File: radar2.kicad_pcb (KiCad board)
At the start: 4 copper layers, 103.4 x 65 mm, 135 parts, among them IC1 BQ25713RSNR, IC2 TPS54540DDA, IC3 LP5907QMFX-3.0Q1, IC5 LP5907QMFX-3.0Q1, IC6 DW3220TR13, J1 GSB1C4621DS1HR, J2 M20-8770546 (for SWD), J3 M20-9730446_DISPLAY_POWER, J4 JST-XH, J5 M20-9990646_PI, J6 SMA_CONNECTOR, J7 SMA_CONNECTOR, Q1 CSD17308Q3, Q2 CSD17308Q3, Q3 CSD17308Q3, Q4 CSD17308Q3, Q5 CSD25404Q3, SW1 09.03290.01, SW2 SWT0220-016016GSA, U1 STM32H725ZETx, Y1 ECS-384-CDX-2482

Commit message: finalizing routing on our battery charger BQ, moving on to GND and completing power routing
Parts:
- moved R17 6.72 mm to (184.6, 101.4), turned to 90 degrees
- moved R18 5.34 mm to (187.0, 101.7), turned to -90 degrees
- moved C31 3.09 mm to (186.2, 99.8)
- moved R1 2.82 mm to (170.3, 97.7)
- moved C3 2.15 mm to (174.3, 97.6)
- moved C2 1.99 mm to (173.5, 99.7)
- moved R16 1.54 mm to (186.2, 98.5)
- moved R11 1.45 mm to (166.2, 98.6)
- moved R2 1.41 mm to (172.8, 97.6), turned to -90 degrees
- moved C1 1.40 mm to (169.2, 97.2)
- moved C10 1.09 mm to (168.1, 97.1)
- moved C30 0.94 mm to (182.2, 99.2), turned to 0 degrees
- moved R6 0.86 mm to (165.3, 93.0)
- moved C5 0.65 mm to (176.4, 98.2)
- moved R3 0.55 mm to (175.3, 95.8)
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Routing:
- net BQ_SDA: track 7.59 -> 96.9 mm, vias 0 -> 2
- net BQ_PROCHOT: track 5.63 -> 91.1 mm, vias 0 -> 2
- net BQ_SCL: track 9.04 -> 92.7 mm, vias 0 -> 2
- net BQ_CHRG_OK: track 5.80 -> 77.9 mm, vias 0 -> 2
- net VBUS: track 17.7 -> 55.9 mm
- net /pmics/ACP: track 1.90 -> 23.9 mm, vias 0 -> 2
- net /pmics/SRN: track 0.00 -> 19.4 mm, vias 0 -> 2
- net /pmics/nBATDRV: track 0.00 -> 19.1 mm, vias 0 -> 2
- net /pmics/SRP: track 0.00 -> 19.1 mm
- net /pmics/ACN: track 3.52 -> 20.5 mm, vias 1 -> 2
- net BATT+: track 11.4 -> 0.00 mm
- net /pmics/VDDA: track 0.00 -> 6.62 mm
- net /pmics/ILIM_HIZ: track 0.00 -> 5.31 mm, vias 0 -> 2
- net Net-(IC1-CELL_BATPRESZ): track 0.00 -> 5.09 mm
- net Net-(IC1-IADPT): track 0.00 -> 4.98 mm
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- added copper zone on F.Cu, net BATT+
- added copper zone on F.Cu, net Net-(Q5-D_1)

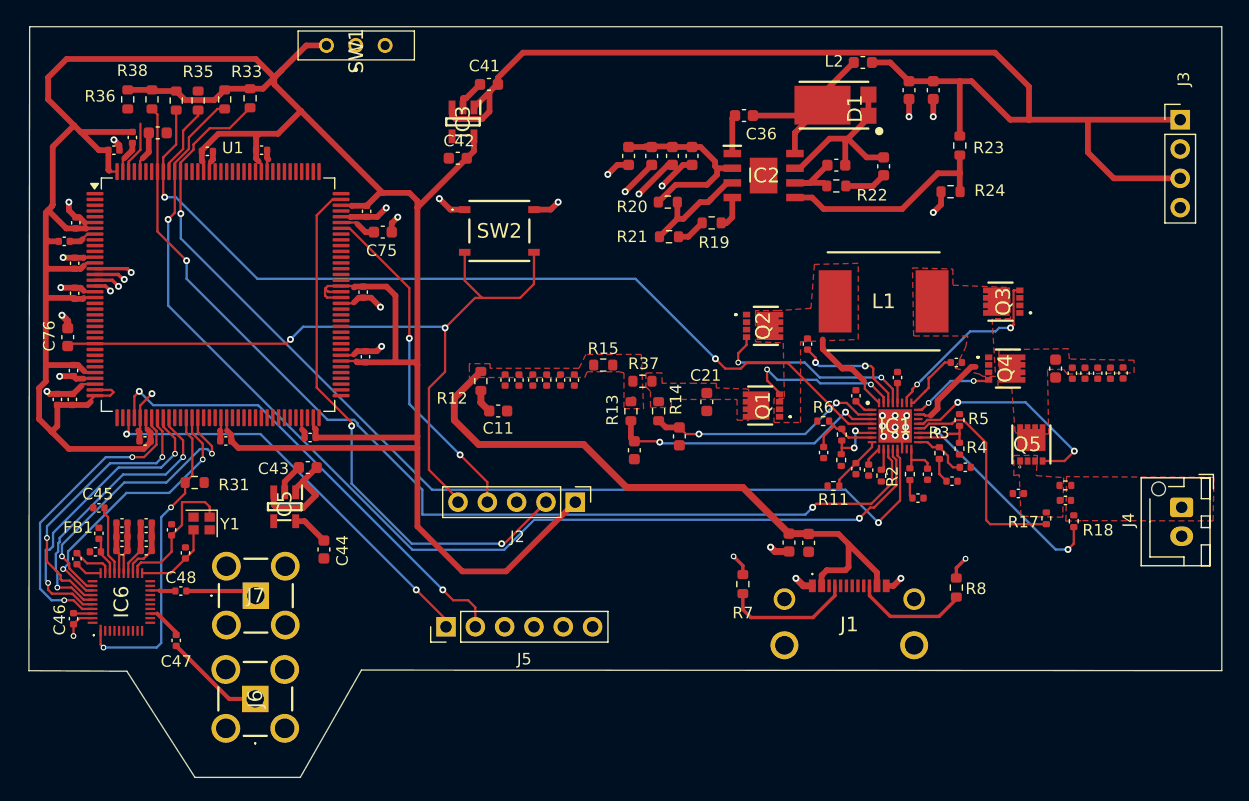
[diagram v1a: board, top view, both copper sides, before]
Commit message: making GND pours and via clusters
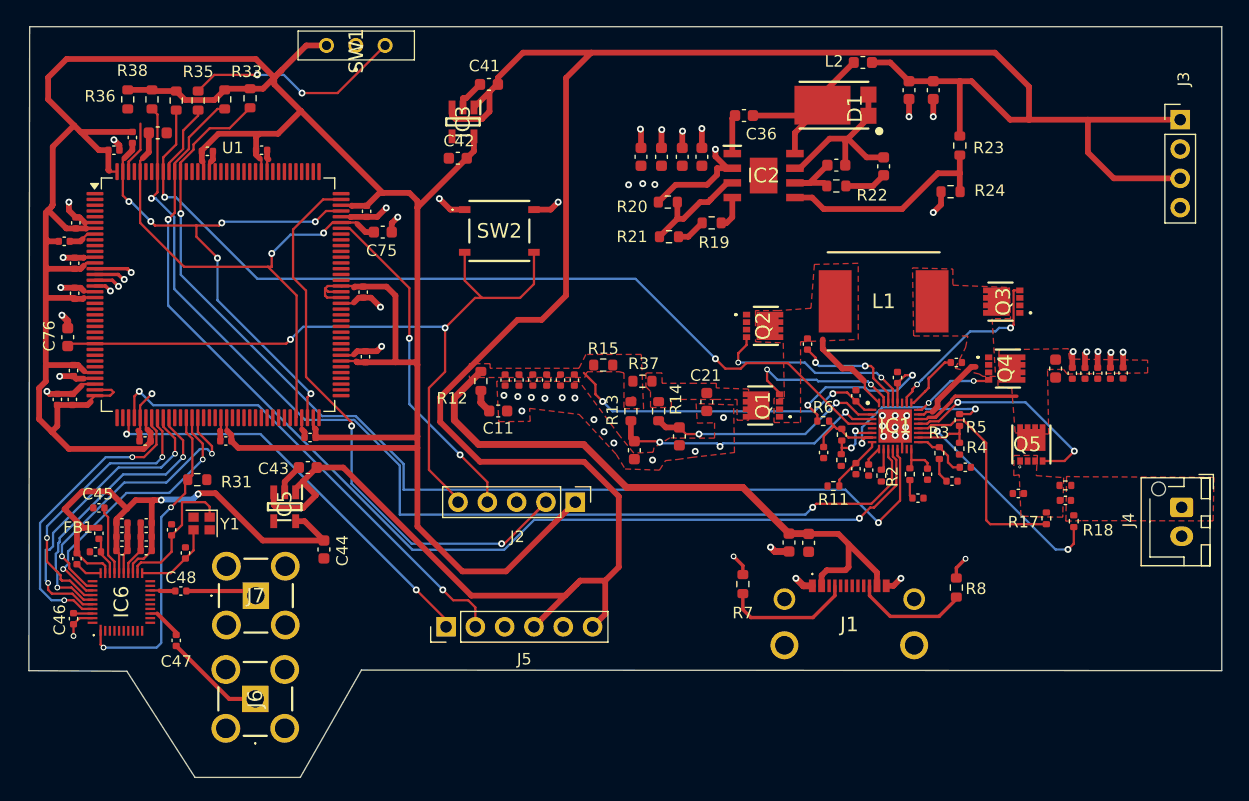
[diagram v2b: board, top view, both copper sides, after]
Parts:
- moved C32 1.08 mm to (149.5, 70.1)
- moved C34 0.85 mm to (153.1, 70.1)
- moved C33 0.85 mm to (151.2, 70.1)
- moved C35 0.85 mm to (154.8, 70.1)
- moved R31 0.34 mm to (111.0, 98.0)
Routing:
- net VOUT_5V: track 115.7 -> 220.5 mm
- net VDDLDO: track 2.82 -> 46.3 mm, vias 0 -> 6
- net Net-(C73-Pad1): track 6.85 -> 46.7 mm, vias 0 -> 2
- net 3V3_RADAR: track 16.4 -> 52.3 mm, vias 0 -> 2
- net VBUS: track 55.9 -> 82.4 mm, vias 0 -> 2
- net Net-(SW1-B): track 0.00 -> 19.1 mm, vias 0 -> 2
- net /pmics/VSYS: track 17.1 -> 33.2 mm, vias 0 -> 10
- net /pmics/VDDA: track 6.62 -> 21.4 mm, vias 0 -> 2
- net /pmics/REGN: track 1.55 -> 15.2 mm, vias 0 -> 2
- net GND: track 125.6 -> 112.8 mm, vias 40 -> 52
- net BQ_SCL: track 92.7 -> 95.9 mm
- net BQ_PROCHOT: track 91.1 -> 94.1 mm
- net ST_JTCLK: track 49.2 -> 51.4 mm
- net /pmics/ACP: track 23.9 -> 24.2 mm, vias 2 -> 3
- added copper zone on In2.Cu, net /pmics/VSYS
- added copper zone on F.Cu, net GND

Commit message: adding keep out zone for our rf ic, 38 unrouted
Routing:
- net GND: track 112.8 -> 128.8 mm, vias 52 -> 85
- net /pmics/VSYS: track 33.2 -> 37.7 mm, vias 10 -> 11
- net VOUT_5V: track 220.5 -> 222.3 mm
- net DW_SPICLK: track 24.5 -> 25.1 mm
- net DW_SPIMISO: track 26.8 -> 27.4 mm

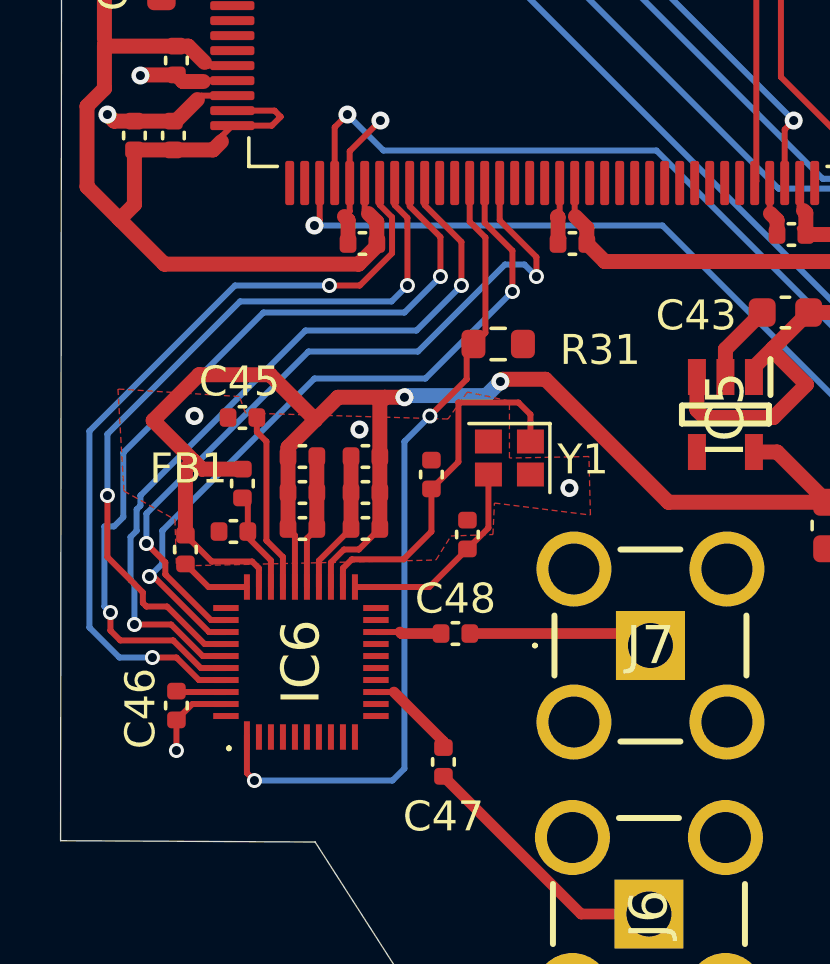
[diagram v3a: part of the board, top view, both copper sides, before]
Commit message: adding gnd vias aorund our rf ic
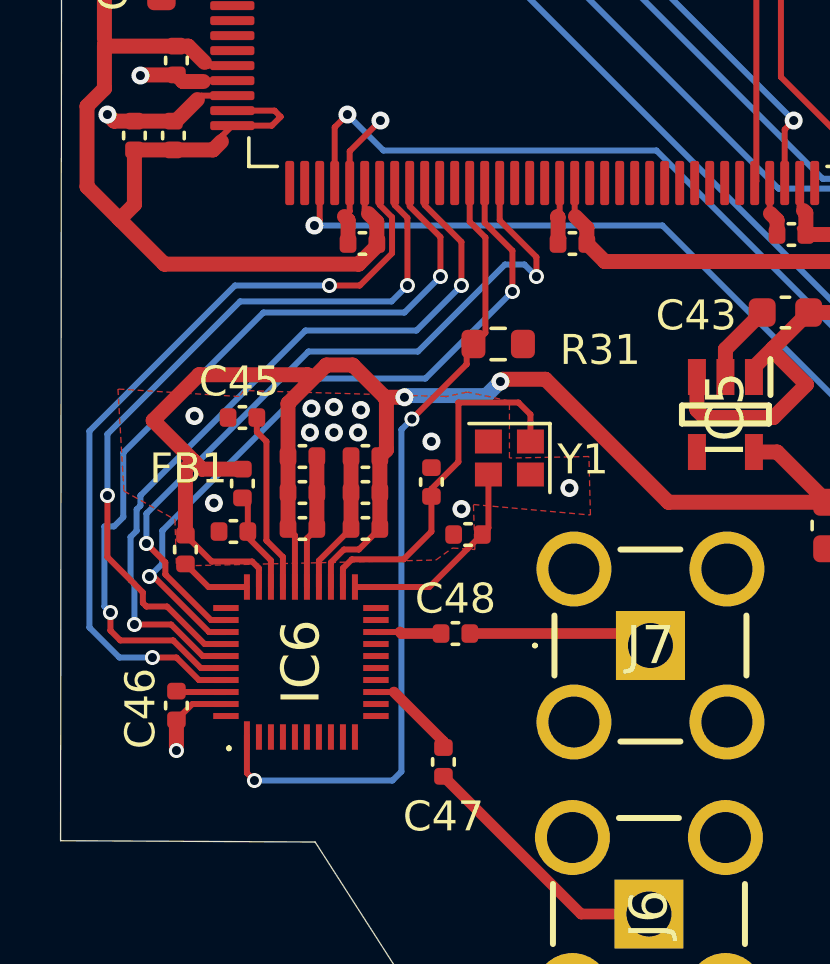
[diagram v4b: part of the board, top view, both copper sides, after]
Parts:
- moved C55 0.25 mm to (108.8, 102.7)
- turned C54 to 180 degrees
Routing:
- net 3V3_RADAR: track 52.3 -> 53.4 mm
- net GND: vias 85 -> 93

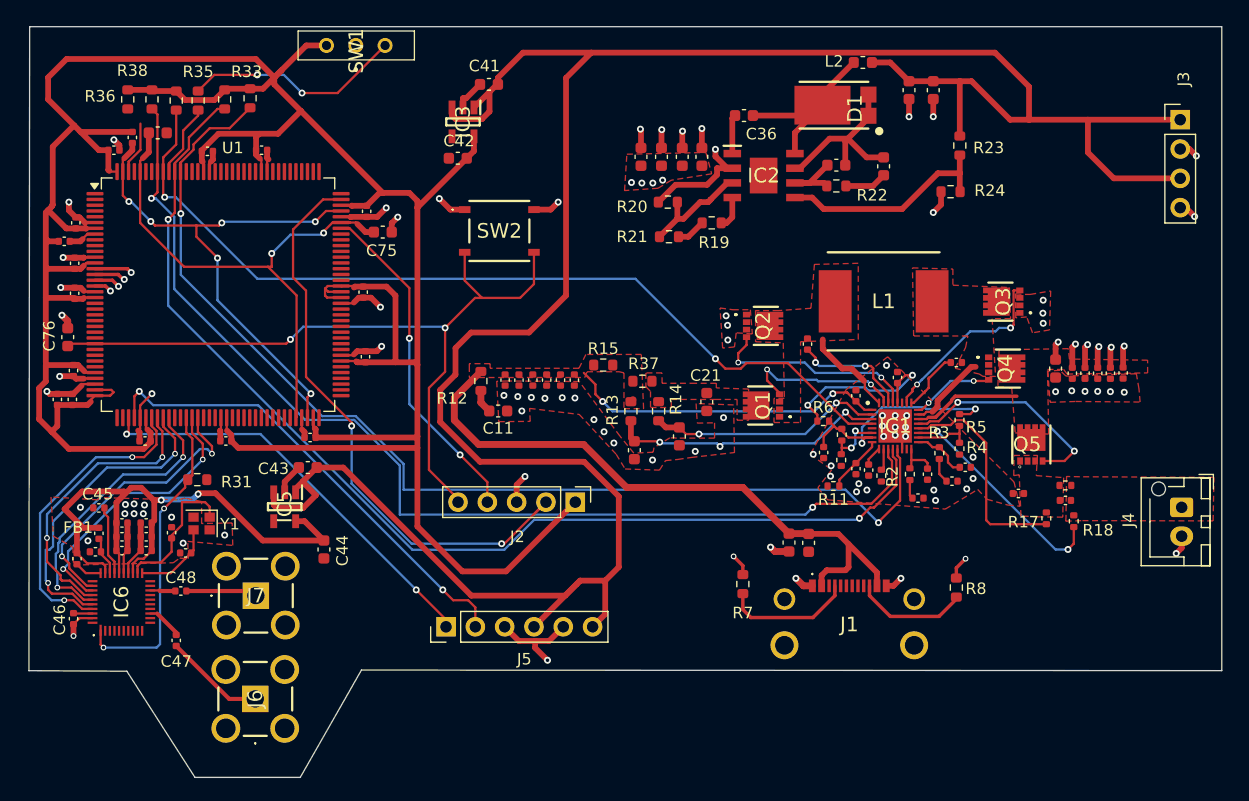
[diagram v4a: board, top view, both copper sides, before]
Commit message: updating pic, 0 unrouted and adding text to our pin headers
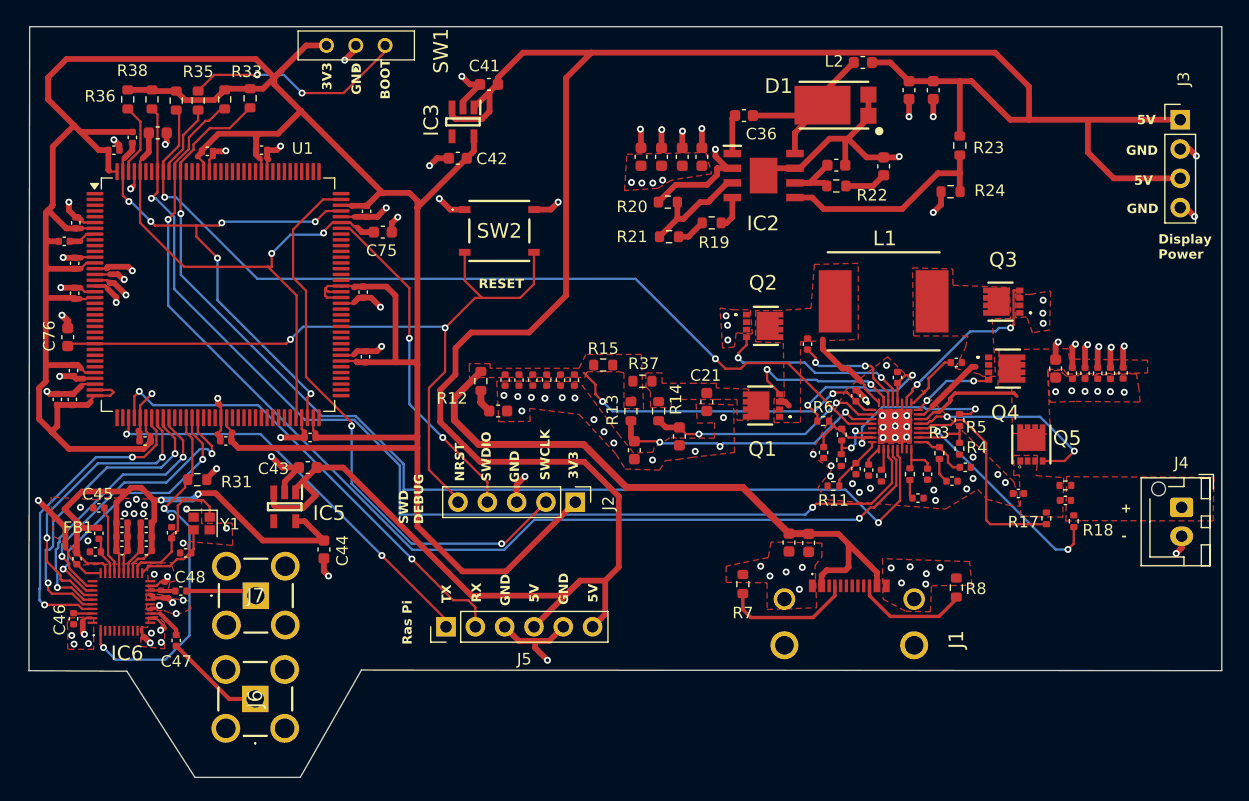
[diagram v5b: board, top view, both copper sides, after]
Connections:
- Q5 pad 9: (no net) -> /pmics/VSYS
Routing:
- net GND: track 128.8 -> 164.0 mm, vias 93 -> 130
- net DW_IRQ: track 27.6 -> 31.8 mm
- net Net-(U1-PDR_ON): track 4.58 -> 6.31 mm
- net /pmics/nBATDRV: track 19.1 -> 18.1 mm
- net /pmics/SW1: track 8.06 -> 8.85 mm
- net DW_SPICSN: track 26.9 -> 27.5 mm
- net Net-(C48-Pad2): track 6.19 -> 5.62 mm
- net /pmics/VSYS: track 37.7 -> 38.2 mm
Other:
- board text added: "+"
- board text added: "-"
- board text added: "3V3"
- board text added: "5V"
- board text added: "BOOT"
- board text added: "Display Power"
- board text added: "GND"
- board text added: "NRST"
- board text added: "RESET"
- board text added: "RX"
- board text added: "Ras Pi"
- board text added: "SWCLK"
- board text added: "SWD DEBUG"
- board text added: "SWDIO"
- board text added: "TX"

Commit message: replacing our indcutr for TPS with proper one, creating a bom tool for easier component selection and fitering, currently getting all my passives in order
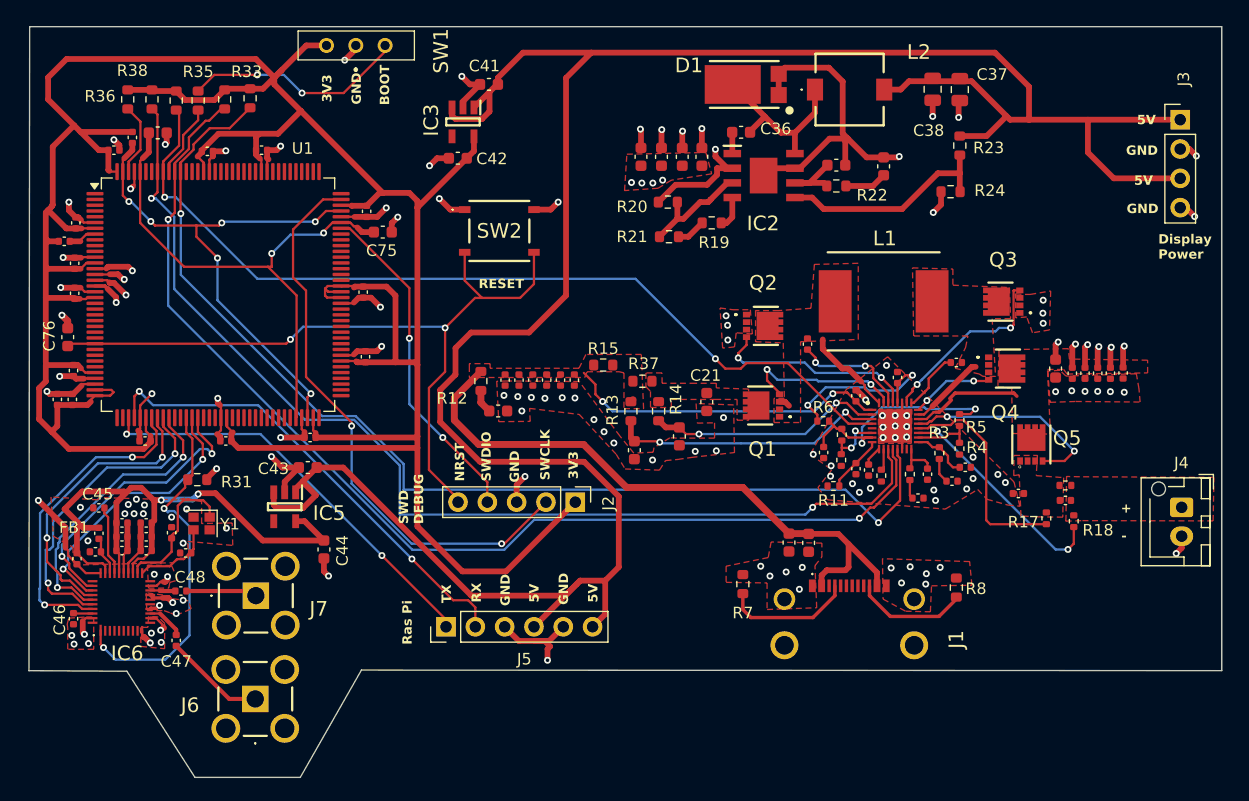
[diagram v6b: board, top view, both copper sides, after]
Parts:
- C37, C38: footprint Capacitor_SMD:C_0603_1608Metric -> Capacitor_SMD:C_0805_2012Metric
- C6: value 0.1muF -> 0.1uF
- C7: value 22muF -> 22uF
- L2: footprint Inductor_SMD:L_0603_1608Metric -> 55induct:CDRH62BNP5R5NCB
- moved D1 7.98 mm to (157.4, 63.8)
- moved L2 2.62 mm to (167.6, 64.2), turned to -90 degrees
- moved C37 2.30 mm to (177.1, 64.2)
- moved C38 2.05 mm to (174.8, 64.2)
- moved C36 1.47 mm to (158.2, 68.0)
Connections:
- Q5 pad 9: /pmics/VSYS -> (no net)
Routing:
- net GND: track 164.0 -> 173.4 mm, vias 130 -> 131
- net Net-(IC2-BOOT): track 3.39 -> 1.85 mm
- net ST_JTCLK: track 51.4 -> 49.9 mm
- net VOUT_5V: track 222.3 -> 220.8 mm
- net /pmics/SW_1: track 16.4 -> 15.3 mm
- net /pmics/ACP: track 24.2 -> 23.9 mm, vias 3 -> 2

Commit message: adding fab files, wow this repo is getting messy
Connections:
- Q5 pad 9: (no net) -> /pmics/VSYS
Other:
- board text added: "Chad was here 8/2026"
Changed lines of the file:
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@@
     )
     (pad_to_mask_clearance 0)
-    (solder_mask_min_width 0.12)
     (grid_origin 158.55 107.35)
     (pcbplotparams
@@
       (plot_on_all_layers_selection 0x0000000_00000000)
       (disableapertmacros false)
-      (usegerberextensions false)
-      (usegerberattributes true)
-      (usegerberadvancedattributes true)
-      (creategerberjobfile true)
+      (usegerberextensions true)
+      (usegerberattributes false)
+      (usegerberadvancedattributes false)
+      (creategerberjobfile false)
       (dashed_line_dash_ratio 12.000000)
       (dashed_line_gap_ratio 3.000000)
@@
       (psa4output false)
       (plotreference true)
-      (plotvalue true)
+      (plotvalue false)
       (plotinvisibletext false)
       (sketchpadsonfab false)
-      (subtractmaskfromsilk false)
+      (subtractmaskfromsilk true)
       (outputformat 1)
       (mirror false)
-      (drillshape 1)
+      (drillshape 0)
       (scaleselection 1)
       (outputdirectory "")
@@
       (stroke (width 0.1) (type solid)) (layer "F.Fab"))
     (pad "" np_thru_hole circle (at -1.6 2 270) (size 1.2 1.2) (drill 1.2) (layers "*.Cu" "*.Mask"))
-    (pad "1" thru_hole roundrect (at 0 0 270) (size 1.7 2) (drill 1) (layers "*.Cu" "*.Mask") (roundrect_rratio 0.147059)
+    (pad "1" thru_hole roundrect (at 0 0 270) (size 1.7 2) (drill 1) (layers "*.Cu" "*.Mask") (roundrect_rratio 0.1470588235)
       (net 21 "BATT+") (pinfunction "Pin_1") (pintype "passive"))
     (pad "2" thru_hole oval (at 2.5 0 270) (size 1.7 2) (drill 1) (layers "*.Cu" "*.Mask")
@@
     (pad "2" smd rect (at 0 -3) (size 1.4 1.9) (layers "F.Cu" "F.Paste" "F.Mask")
       (net 173 "VOUT_5V") (pinfunction "2") (pintype "passive"))
-    (model "${KIPRJMOD}/components/passive/CDRH62BNP-5R5NC-B.stp"
+    (model "CDRH62BNP-5R5NC-B.stp"
       (offset (xyz 0 0 0))
       (scale (xyz 1 1 1))
@@
     (pad "8" smd rect (at -0.975 -1.545 90) (size 0.41 0.5) (layers "F.Cu" "F.Paste" "F.Mask")
       (net 19 "/pmics/VSYS") (pinfunction "S_4") (pintype "passive"))
-    (pad "9" smd rect (at 0 -0.39 90) (size 1.9 2.45) (layers "F.Cu" "F.Paste" "F.Mask"))
+    (pad "9" smd rect (at 0 -0.39 90) (size 1.9 2.45) (layers "F.Cu" "F.Paste" "F.Mask")
+      (net 19 "/pmics/VSYS"))
     (model "${KIPRJMOD}/components/pmics/csd254/CSD25404Q3.stp"
       (offset (xyz 0 0 0))
@@
     (pad "2" smd rect (at 4.2 0) (size 2.85 5.4) (layers "F.Cu" "F.Paste" "F.Mask")
       (net 18 "/pmics/SW2") (pinfunction "2") (pintype "passive"))
-    (model "${KIPRJMOD}/components/passive/induct.stp"
+    (model "74437356022.stp"
       (offset (xyz 0 0 0.04999999999))
       (scale (xyz 1 1 1))
@@
   (gr_line (start 119.95 123.85) (end 125.25 114.55)
     (stroke (width 0.0381) (type default)) (layer "Edge.Cuts"))
+  (gr_text "Chad was here\n8/2026" (at 192.55 110.25) (layer "B.SilkS")
+    (effects (font (size 0.8128 0.8128) (thickness 0.1524) bold) (justify left bottom mirror))
+  )
   (gr_text "3V3\n" (at 122.75 65.35 90) (layer "F.SilkS")
     (effects (font (size 0.8128 0.8128) (thickness 0.1524) bold) (justify left bottom))

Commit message: updating pcb pic
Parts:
- moved J4 4.15 mm to (192.2, 100.0)
- moved J3 3.29 mm to (192.9, 66.4)
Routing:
- net VOUT_5V: track 220.8 -> 214.7 mm
- net GND: track 173.4 -> 174.7 mm
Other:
- board size 103.4 x 65 mm -> 99.5 x 65 mm
